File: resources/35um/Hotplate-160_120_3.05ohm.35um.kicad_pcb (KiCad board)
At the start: 2 copper layers, 160 x 120 mm, 7 parts, among them J1 Hotplate_Power_Connection, J2 Hotplate_Power_Connection

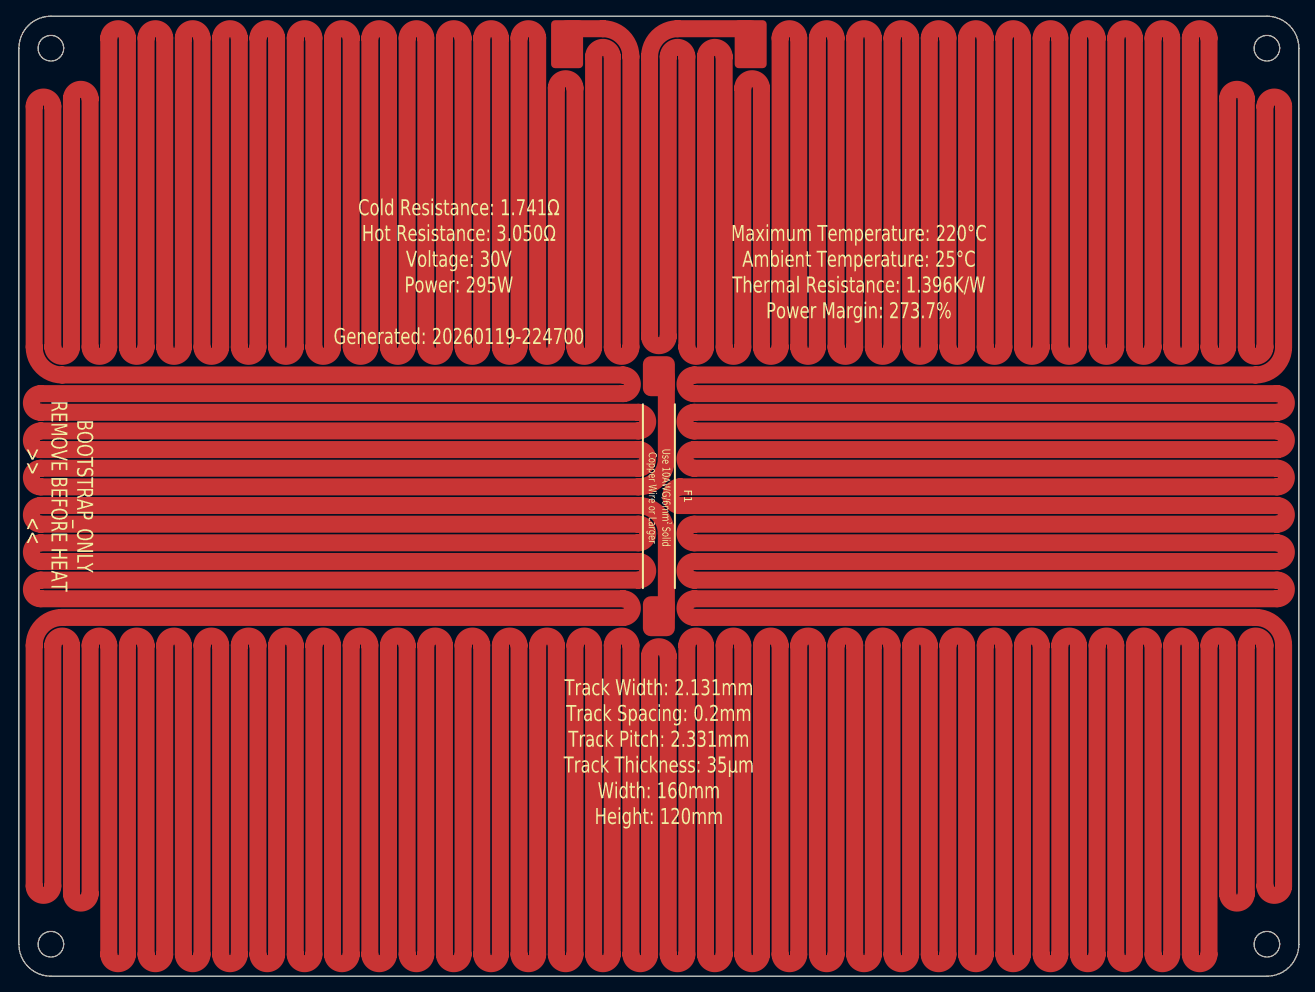
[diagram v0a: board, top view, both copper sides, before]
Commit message: Updated bootstrap jumper to not straddle multiple nets and include a solder mask dam between the jumper pads.
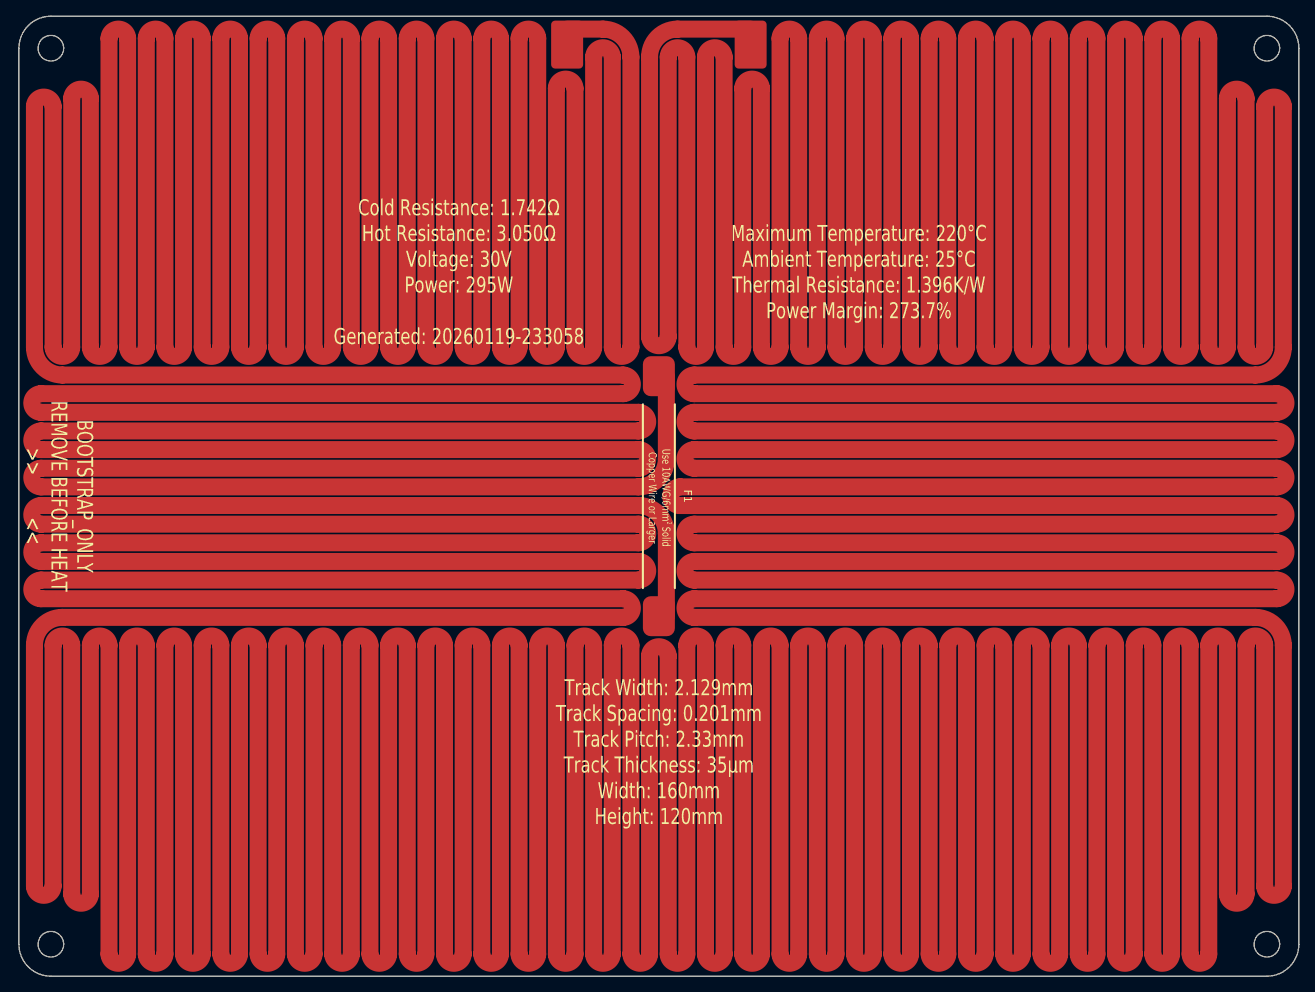
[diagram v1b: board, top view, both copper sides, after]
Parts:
- moved J1 0.05 mm to (93.5, 48.5)
- moved J2 0.05 mm to (116.5, 48.5)
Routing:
- net Net-(J2-Pin_1): track 5828.0 -> 5823.3 mm
- net Net-(J1-Pin_1): track 1895.3 -> 1893.9 mm
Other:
- board text added: "Cold Resistance: 1.742Ω Hot Resistance: 3.050Ω Voltage: 30V Power: 295W Generated: 20260119-233058"
- board text added: "Track Width: 2.129mm Track Spacing: 0.201mm Track Pitch: 2.33mm Track Thickness: 35µm Width: 160mm Height: 120mm"
- board text removed: "Cold Resistance: 1.741Ω Hot Resistance: 3.050Ω Voltage: 30V Power: 295W Generated: 20260119-224700"
- board text removed: "Track Width: 2.131mm Track Spacing: 0.2mm Track Pitch: 2.331mm Track Thickness: 35µm Width: 160mm Height: 120mm"
